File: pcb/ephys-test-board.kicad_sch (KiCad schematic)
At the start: 9 parts, among them J1 10129383-910002ALF, J8 BM03B-SRSS-TB

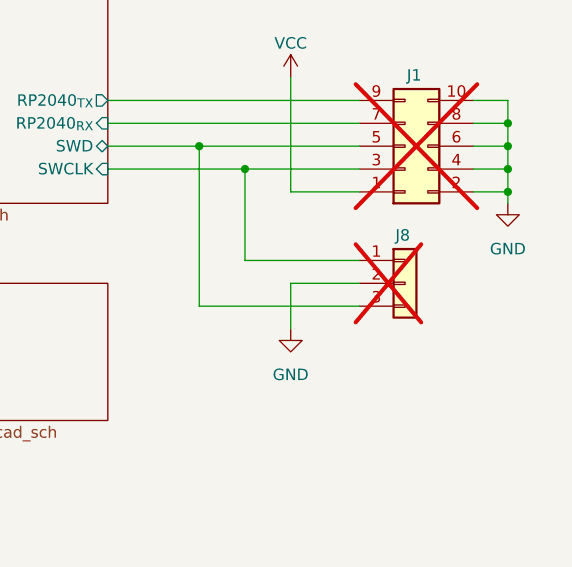
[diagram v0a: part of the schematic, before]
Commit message: 1st step OEPSPN & MPN on components
- still missing new codes to be emitted
- project/schematic/components not tunned with Jon's project at this date
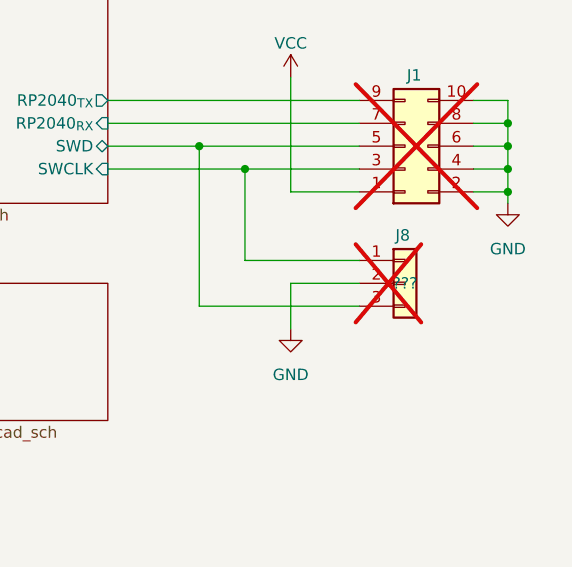
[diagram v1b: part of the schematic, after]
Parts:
- J1, TP11, TP12: now left out of the parts list
- J8: OEPSPN (none) -> ???; now left out of the parts list
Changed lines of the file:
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@@
 			)
 		)
-		(property "Datasheet1" ""
+		(property "Tolerance" ""
 			(at 250.19 153.67 0)
 			(effects
@@
 					(size 1.27 1.27)
 				)
-				(hide yes)
-			)
-		)
-		(property "Part No." ""
-			(at 250.19 153.67 0)
-			(effects
-				(font
-					(size 1.27 1.27)
-				)
-				(hide yes)
-			)
-		)
-		(property "Tolerance" ""
+			)
+		)
+		(property "OEPSPN" ""
 			(at 250.19 153.67 0)
 			(effects
@@
 		(unit 1)
 		(exclude_from_sim no)
-		(in_bom yes)
+		(in_bom no)
 		(on_board yes)
 		(dnp yes)
@@
 			)
 		)
-		(property "Datasheet1" ""
+		(property "Tolerance" ""
 			(at 252.73 97.79 0)
 			(effects
@@
 					(size 1.27 1.27)
 				)
-				(hide yes)
-			)
-		)
-		(property "Part No." ""
-			(at 252.73 97.79 0)
-			(effects
-				(font
-					(size 1.27 1.27)
-				)
-				(hide yes)
-			)
-		)
-		(property "Tolerance" ""
+			)
+		)
+		(property "OEPSPN" ""
 			(at 252.73 97.79 0)
 			(effects
@@
 			)
 		)
-		(property "Datasheet1" ""
+		(property "Tolerance" ""
 			(at 236.22 151.13 0)
 			(effects
@@
 					(size 1.27 1.27)
 				)
-				(hide yes)
-			)
-		)
-		(property "Part No." ""
-			(at 236.22 151.13 0)
-			(effects
-				(font
-					(size 1.27 1.27)
-				)
-				(hide yes)
-			)
-		)
-		(property "Tolerance" ""
+			)
+		)
+		(property "OEPSPN" ""
 			(at 236.22 151.13 0)
 			(effects
@@
 			)
 		)
-		(property "Datasheet1" ""
+		(property "Tolerance" ""
 			(at 201.93 151.13 0)
 			(effects
@@
 					(size 1.27 1.27)
 				)
-				(hide yes)
-			)
-		)
-		(property "Part No." ""
-			(at 201.93 151.13 0)
-			(effects
-				(font
-					(size 1.27 1.27)
-				)
-				(hide yes)
-			)
-		)
-		(property "Tolerance" ""
+			)
+		)
+		(property "OEPSPN" ""
 			(at 201.93 151.13 0)
 			(effects
@@
 			)
 		)
-		(property "Datasheet1" ""
+		(property "Tolerance" ""
 			(at 213.36 151.13 0)
 			(effects
@@
 					(size 1.27 1.27)
 				)
-				(hide yes)
-			)
-		)
-		(property "Part No." ""
-			(at 213.36 151.13 0)
-			(effects
-				(font
-					(size 1.27 1.27)
-				)
-				(hide yes)
-			)
-		)
-		(property "Tolerance" ""
+			)
+		)
+		(property "OEPSPN" ""
 			(at 213.36 151.13 0)
 			(effects
@@
 		(unit 1)
 		(exclude_from_sim no)
-		(in_bom yes)
+		(in_bom no)
 		(on_board yes)
 		(dnp yes)
@@
 			)
 		)
-		(property "Datasheet1" ""
-			(at 252.73 113.03 0)
-			(effects
-				(font
-					(size 1.27 1.27)
-				)
-				(hide yes)
-			)
-		)
-		(property "Part No." ""
-			(at 252.73 113.03 0)
-			(effects
-				(font
-					(size 1.27 1.27)
-				)
-				(hide yes)
-			)
-		)
 		(property "Tolerance" ""
 			(at 252.73 113.03 0)
@@
 			)
 		)
+		(property "OEPSPN" "???"
+			(at 252.73 113.03 0)
+			(effects
+				(font
+					(size 1.27 1.27)
+				)
+			)
+		)
 		(pin "2"
 		)
@@
 		(unit 1)
 		(exclude_from_sim no)
-		(in_bom yes)
+		(in_bom no)
 		(on_board yes)
 		(dnp no)
@@
 			)
 		)
-		(property "Datasheet1" ""
+		(property "Tolerance" ""
 			(at 190.5 25.4 0)
 			(effects
@@
 					(size 1.27 1.27)
 				)
-				(hide yes)
-			)
-		)
-		(property "Part No." ""
-			(at 190.5 25.4 0)
-			(effects
-				(font
-					(size 1.27 1.27)
-				)
-				(hide yes)
-			)
-		)
-		(property "Tolerance" ""
+			)
+		)
+		(property "OEPSPN" ""
 			(at 190.5 25.4 0)
 			(effects
@@
 			)
 		)
-		(property "Datasheet1" ""
-			(at 224.79 151.13 0)
-			(effects
-				(font
-					(size 1.27 1.27)
-				)
-				(hide yes)
-			)
-		)
-		(property "Part No." ""
-			(at 224.79 151.13 0)
-			(effects
-				(font
-					(size 1.27 1.27)
-				)
-				(hide yes)
-			)
-		)
 		(property "Tolerance" ""
 			(at 224.79 151.13 0)
@@
 			)
 		)
+		(property "OEPSPN" ""
+			(at 224.79 151.13 0)
+			(effects
+				(font
+					(size 1.27 1.27)
+				)
+			)
+		)
 		(pin "1"
 		)
@@
 		(unit 1)
 		(exclude_from_sim no)
-		(in_bom yes)
+		(in_bom no)
 		(on_board yes)
 		(dnp no)
@@
 			)
 		)
-		(property "Datasheet1" ""
-			(at 182.88 25.4 0)
-			(effects
-				(font
-					(size 1.27 1.27)
-				)
-				(hide yes)
-			)
-		)
-		(property "Part No." ""
-			(at 182.88 25.4 0)
-			(effects
-				(font
-					(size 1.27 1.27)
-				)
-				(hide yes)
-			)
-		)
 		(property "Tolerance" ""
 			(at 182.88 25.4 0)
 			(effects
+				(font
+					(size 1.27 1.27)
+				)
+			)
+		)
+		(property "OEPSPN" ""
+			(at 182.88 25.4 0)
+			(effects

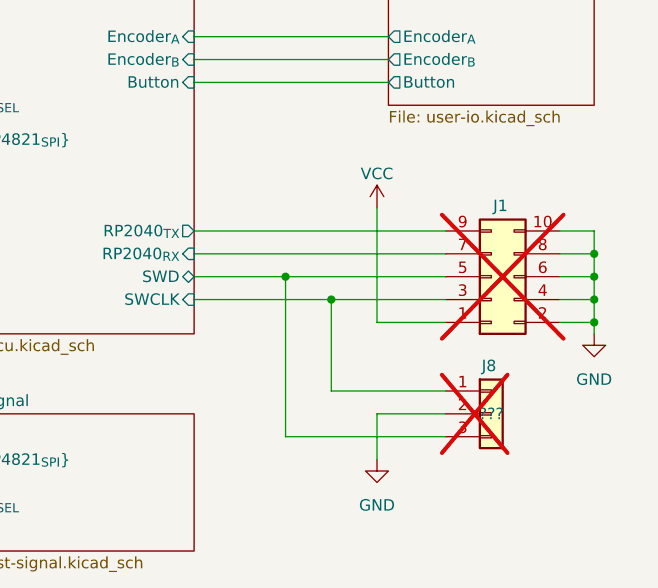
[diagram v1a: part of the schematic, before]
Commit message: tunned with Main branch
- OEPSPN & MPN already on components
- missing 4 these codes
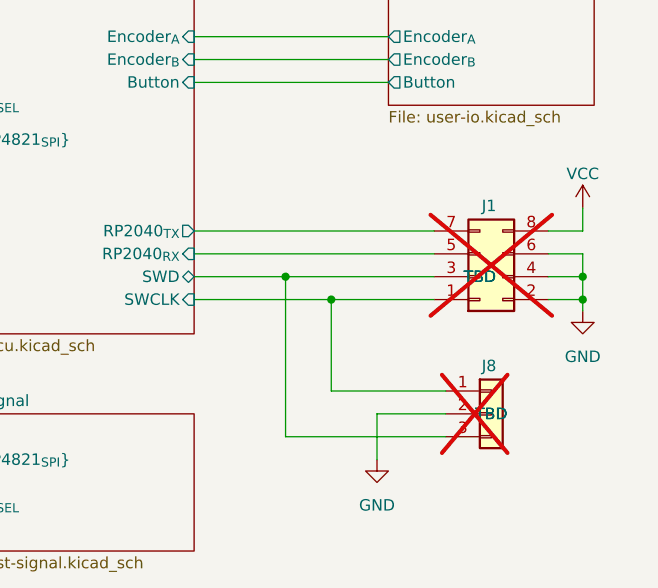
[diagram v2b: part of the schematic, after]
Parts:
- J1: footprint Connector_PinHeader_2.54mm:PinHeader_2x05_P2.54mm_Vertical_SMD -> Connector_PinHeader_2.54mm:PinHeader_2x04_P2.54mm_Vertical_SMD; symbol Connector_Generic:Conn_02x05_Odd_Even -> Connector_Generic:Conn_02x04_Odd_Even; MPN (none) -> TBD; OEPSPN (none) -> TBD; now in the parts list
- J8: MPN (none) -> TBD; OEPSPN ??? -> TBD; now in the parts list
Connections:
- net GND: no longer J1.10 (Pin_10), J1.8 (Pin_8)
- net MCU/RP2040_{RX}: now also J1.5 (Pin_5); no longer J1.7 (Pin_7)
- net MCU/RP2040_{TX}: now also J1.7 (Pin_7); no longer J1.9 (Pin_9)
- net MCU/SWCLK: now also J1.1 (Pin_1); no longer J1.3 (Pin_3)
- net MCU/SWD: now also J1.3 (Pin_3); no longer J1.5 (Pin_5)
- net VCC: now also J1.8 (Pin_8); no longer J1.1 (Pin_1)
